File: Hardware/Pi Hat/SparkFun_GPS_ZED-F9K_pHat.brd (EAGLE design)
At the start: 65 x 56.5 mm, 73 parts, among them J1 QWIIC_RIGHT_ANGLE, J2 RASPBERRYPI-40-PIN-GPIO_PTH_N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, J4 U.FL, U1 UBLOX_ZED_F9K, U3 TRIPLE_BUFFER_74LVC3G07

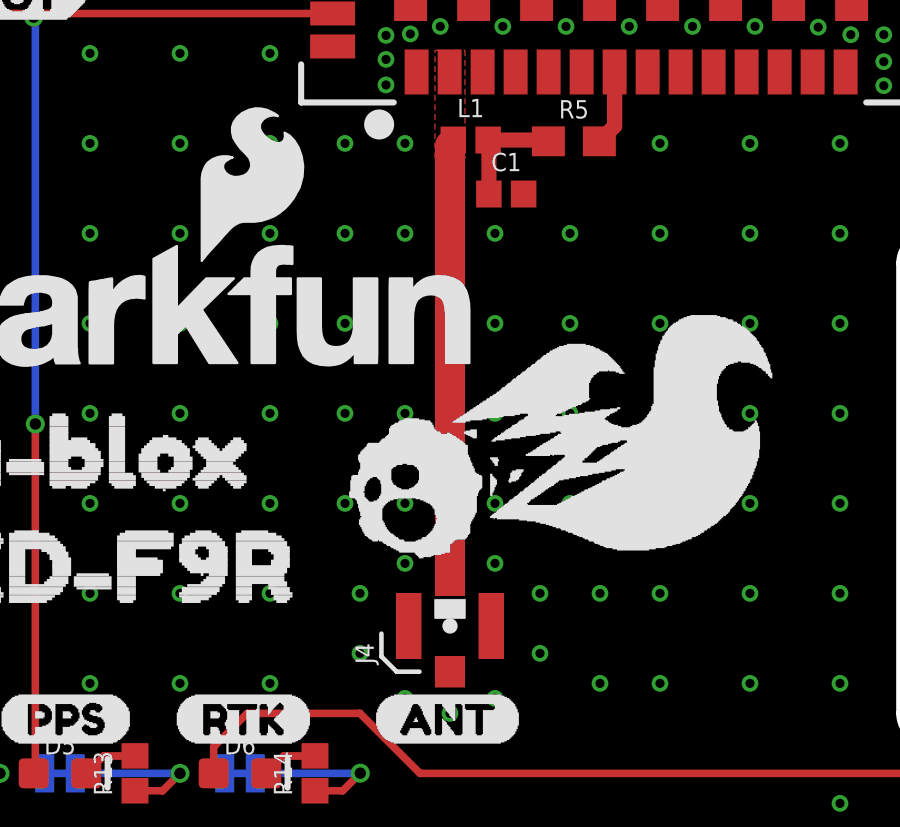
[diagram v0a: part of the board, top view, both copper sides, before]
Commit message: Moves buzzard labels to their own folder - updates breakout board with better labeling
* fixes I2C lines being backwards
* Moves D+ and D- lines around
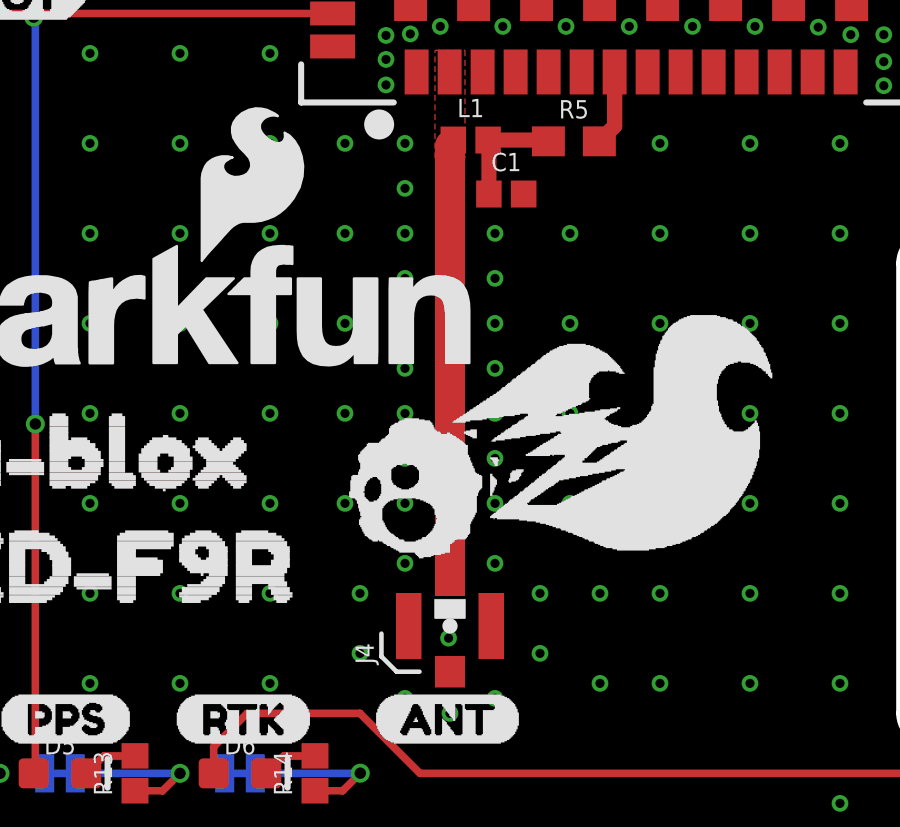
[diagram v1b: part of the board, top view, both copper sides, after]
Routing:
- net GND: vias 282 -> 290
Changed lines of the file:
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@@
 <setting verticaltext="up"/>
 </settings>
-<grid distance="1" unitdist="mm" unit="mm" style="lines" multiple="1" display="yes" altdistance="0.05" altunitdist="mm" altunit="mm"/>
+<grid distance="1" unitdist="mm" unit="mm" style="lines" multiple="1" display="yes" altdistance="0.5" altunitdist="mm" altunit="mm"/>
 <layers>
 <layer number="1" name="Top" color="4" fill="1" visible="yes" active="yes"/>
@@
 <layer number="115" name="ReferenceISLANDS" color="7" fill="1" visible="no" active="no"/>
 <layer number="116" name="Patch_BOT" color="9" fill="4" visible="no" active="no"/>
-<layer number="117" name="PM_Ref" color="26" fill="1" visible="yes" active="yes"/>
+<layer number="117" name="PM_Ref" color="26" fill="1" visible="no" active="yes"/>
 <layer number="118" name="Rect_Pads" color="7" fill="1" visible="no" active="no"/>
-<layer number="119" name="PF_Ref" color="31" fill="1" visible="yes" active="yes"/>
-<layer number="120" name="WFL_Ref" color="25" fill="1" visible="yes" active="yes"/>
+<layer number="119" name="PF_Ref" color="31" fill="1" visible="no" active="yes"/>
+<layer number="120" name="WFL_Ref" color="25" fill="1" visible="no" active="yes"/>
 <layer number="121" name="_tsilk" color="7" fill="1" visible="no" active="no"/>
 <layer number="122" name="_bsilk" color="7" fill="1" visible="no" active="no"/>
@@
 <via x="27.6766" y="26.6486" extent="1-16" drill="0.3048"/>
 <via x="42.3594" y="26.624" extent="1-16" drill="0.3048"/>
+<via x="28.952" y="6.508" extent="1-16" drill="0.3048"/>
+<via x="30.5" y="15.5" extent="1-16" drill="0.3048"/>
+<via x="27.5" y="15.5" extent="1-16" drill="0.3048"/>
+<via x="27.5" y="18.5" extent="1-16" drill="0.3048"/>
+<via x="30.5" y="18.5" extent="1-16" drill="0.3048"/>
+<via x="27.5" y="21.5" extent="1-16" drill="0.3048"/>
+<via x="27.5" y="12.5" extent="1-16" drill="0.3048"/>
+<via x="30.5" y="12.5" extent="1-16" drill="0.3048"/>
 </signal>
 <signal name="3.3V">

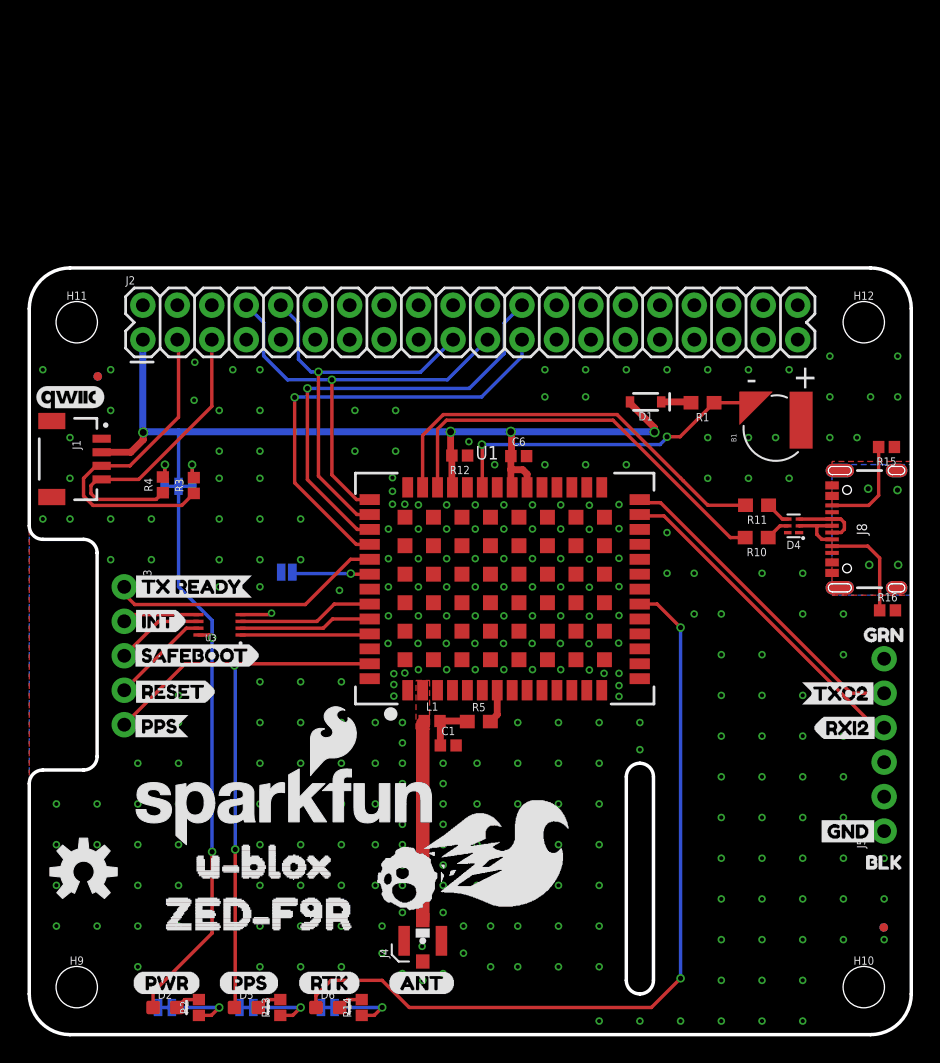
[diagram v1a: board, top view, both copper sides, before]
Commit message: Adjust pi-hat design
* Moves jumpers to teh top
* moves labels for LEDs to teh Edge
* Moves USB and FTDI header to the bottom edge
* Fixes ESD protection IC routing
* Fixes RX/TX
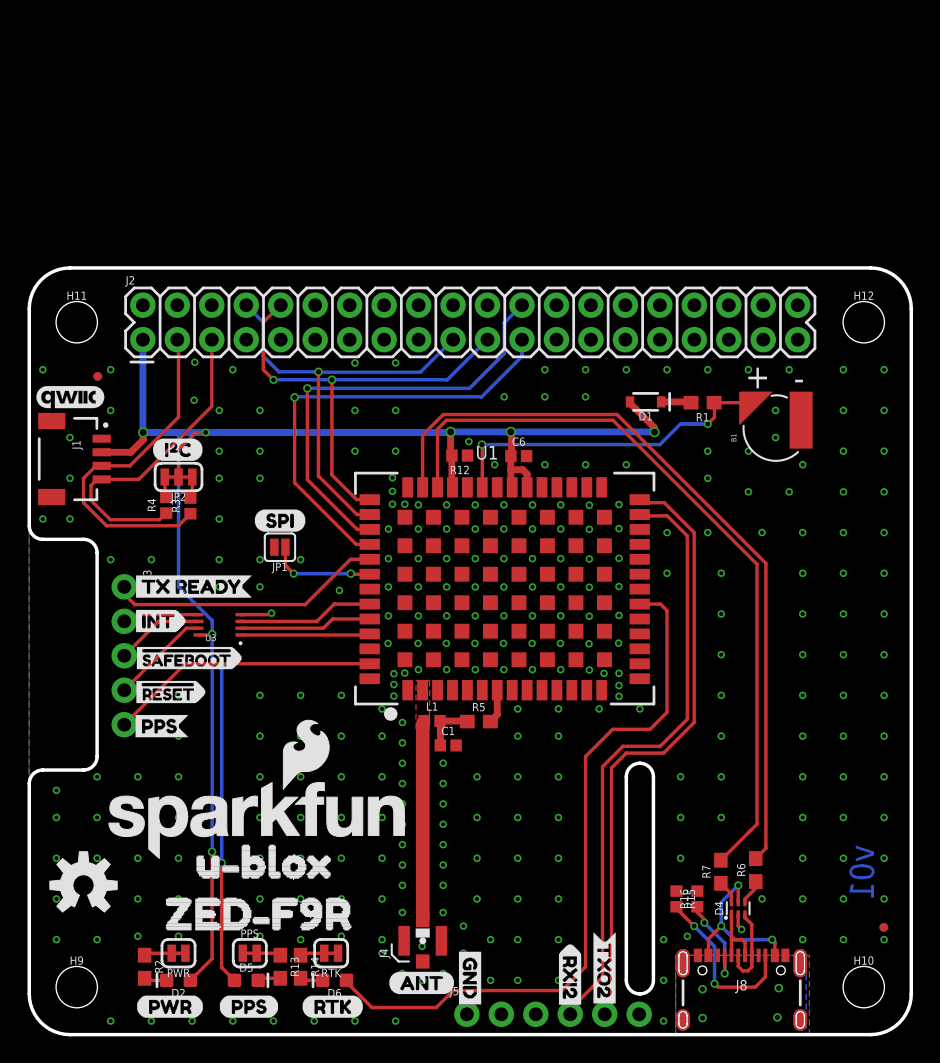
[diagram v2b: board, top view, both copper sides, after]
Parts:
- removed R10, R11: 27, SparkFun-Resistors:0603
- removed U$22: (no value), even_moar:BLK3
- removed U$23: (no value), even_moar:GRN2
- removed U$27: (no value), NEO_GPS_board_silk_FINAL#03#jpg:NEO_GPS_BOARD_SILK_FINAL#03#JPG
- added R6, R7: 27, SparkFun-Resistors:0603
- R13, R14, R2: value 1KOHM-0402-1/16W-1% -> 1k; device SparkFun-Resistors:0402 -> SparkFun-Resistors:0603
- U$13: device bottom labels:RESET4 -> corrected_safe_reset:#SAFEBOOT0
- U$15: device bottom labels:SAFEBOOT3 -> corrected_safe_reset:#SAFEBOOT3
- U$7: device ALL_LABELS:SAFEBOOT2 -> corrected_safe_reset:#RESET1
- U$8: device moar:RESET0 -> corrected_safe_reset:#RESET2
- moved R15 36.7 mm to (47.7, 10.0), turned to 270 degrees
- moved J5 33.6 mm to (32.2, 1.50), turned to 0 degrees
- moved U$19 33.0 mm to (32.5, 1.76), turned to 90 degrees
- moved J8 31.7 mm to (52.5, 6.18), turned to 0 degrees
- moved U$16 31.0 mm to (42.4, 1.76), turned to 90 degrees
- moved U$14 31.0 mm to (39.9, 1.76), turned to 90 degrees
- moved D4 28.5 mm to (52.2, 9.31), turned to 90 degrees
- moved U$18 26.8 mm to (32.5, 6.59), turned to 270 degrees
- moved R16 25.5 mm to (49.2, 10.0), turned to 270 degrees
- moved U$6 23.9 mm to (39.9, 6.72), turned to 270 degrees
- moved U$10 22.7 mm to (42.4, 7.65), turned to 270 degrees
- moved U$24 7.25 mm to (16.5, 37.9), flipped to the top
- moved U$13 6.92 mm to (7.25, 27.8), flipped to the top
- moved U$20 6.15 mm to (9.05, 43.1), flipped to the top
- moved U$8 5.90 mm to (13.2, 25.2), flipped to the bottom
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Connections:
- net USB_D+ renamed N$9
- removed net N$16: D4.5, R10.1
- removed net N$17: D4.4, R11.1
- removed net USB_D-: D4.2, J8.A7, J8.B7
- new net N$10: D4.5, J8.VBUS1, J8.VBUS2
- new net N$11: D4.1, J8.A7, J8.B7
- new net N$14: U1.P22
- new net N$15: U1.P23
- new net N$6: D4.6, R7.1
- new net N$7: D4.4, R6.1
- net DMINUS: now also R7.2; no longer R10.2
- net DPLUS: now also R6.2; no longer R11.2
- net GND: now also D4.2
- net RXI/MOSI: now also J2.8; no longer J2.10
- net TXO/MISO: now also J2.10; no longer J2.8
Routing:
- net DPLUS: track 31.0 -> 56.4 mm
- net DMINUS: track 30.8 -> 55.4 mm
- net TXO2: track 23.9 -> 44.9 mm
- net RXI2: track 24.6 -> 44.7 mm
- net N$10: track 0.00 -> 12.7 mm, vias 0 -> 3
- net RTK_STAT: track 59.5 -> 52.3 mm, vias 2 -> 0
- net N$12: track 7.31 -> 12.6 mm, vias 0 -> 2
- net N$11: track 0.00 -> 5.11 mm
- net USB_D-: track 4.31 -> 0.00 mm
- net N$22: track 5.26 -> 1.80 mm, vias 1 -> 0
- net N$23: track 5.23 -> 1.80 mm, vias 1 -> 0
- net N$8: track 5.23 -> 2.05 mm, vias 1 -> 0
- net RXI/MOSI: track 29.9 -> 32.4 mm
- net D_SEL: track 5.77 -> 7.82 mm, vias 1 -> 2
- net N$7: track 0.00 -> 1.87 mm
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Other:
- board text added: "v01"
